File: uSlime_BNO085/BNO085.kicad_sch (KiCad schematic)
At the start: 12 parts, among them CN1 X1502WR-05K-N0SN, U1 BNO085

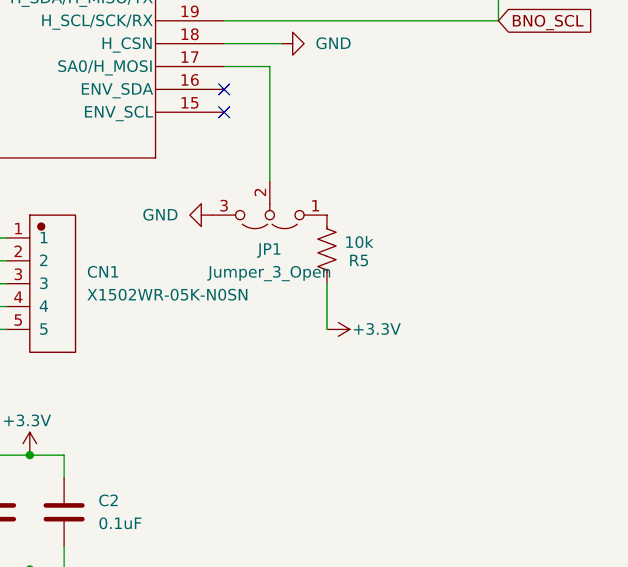
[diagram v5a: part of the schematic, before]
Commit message: Connect DI without resistor
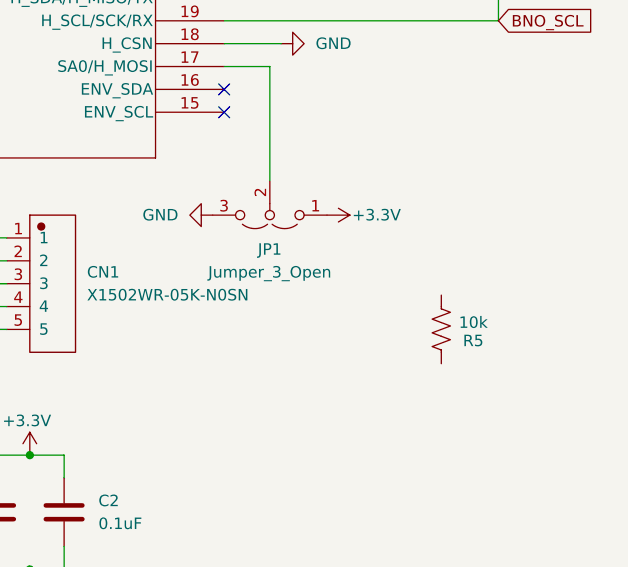
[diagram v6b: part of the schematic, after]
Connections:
- net +3.3V: now also JP1.1 (A); no longer R5.2
- net at R5.1: no longer JP1.1 (A)
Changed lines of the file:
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@@
-	(wire
-		(pts
-			(xy 168.91 119.38) (xy 168.91 114.3)
-		)
-		(stroke
-			(width 0)
-			(type default)
-		)
-	)
 	(wire
 		(pts
@@
 	(symbol
 		(lib_id "power:+3.3V")
-		(at 168.91 119.38 270)
+		(at 168.91 106.68 270)
 		(unit 1)
 		(exclude_from_sim no)
@@
 		(dnp no)
 		(property "Reference" "#PWR014"
-			(at 165.1 119.38 0)
+			(at 165.1 106.68 0)
 			(effects
 				(font
@@
 		)
 		(property "Value" "+3.3V"
-			(at 171.704 119.38 90)
+			(at 171.704 106.68 90)
 			(effects
 				(font
@@
 		)
 		(property "Footprint" ""
-			(at 168.91 119.38 0)
+			(at 168.91 106.68 0)
 			(effects
 				(font
@@
 		)
 		(property "Datasheet" ""
-			(at 168.91 119.38 0)
+			(at 168.91 106.68 0)
 			(effects
 				(font
@@
 		)
 		(property "Description" "Power symbol creates a global label with name \"+3.3V\""
-			(at 168.91 119.38 0)
+			(at 168.91 106.68 0)
 			(effects
 				(font
@@
 				(path "/f32c1c49-f803-4e7c-a530-6db148a7ba36/1072de81-ddaf-4115-9b1e-8b480e2a0117"
 					(reference "#PWR014")
-					(unit 1)
-				)
-			)
-		)
-	)
-	(symbol
-		(lib_id "uSlime:R_US")
-		(at 168.91 110.49 0)
-		(unit 1)
-		(exclude_from_sim no)
-		(in_bom yes)
-		(on_board yes)
-		(dnp no)
-		(property "Reference" "R5"
-			(at 172.466 111.76 0)
-			(effects
-				(font
-					(size 1.27 1.27)
-				)
-			)
-		)
-		(property "Value" "10k"
-			(at 172.466 109.728 0)
-			(effects
-				(font
-					(size 1.27 1.27)
-				)
-			)
-		)
-		(property "Footprint" "Resistor_SMD:R_0402_1005Metric"
-			(at 169.926 110.744 90)
-			(effects
-				(font
-					(size 1.27 1.27)
-				)
-				(hide yes)
-			)
-		)
-		(property "Datasheet" "~"
-			(at 168.91 110.49 0)
-			(effects
-				(font
-					(size 1.27 1.27)
-				)
-				(hide yes)
-			)
-		)
-		(property "Description" "Resistor, US symbol"
-			(at 168.91 110.49 0)
-			(effects
-				(font
-					(size 1.27 1.27)
-				)
-				(hide yes)
-			)
-		)
-		(pin "2"
-		)
-		(pin "1"
-		)
-		(instances
-			(project "uSlime_BNO085"
-				(path "/f32c1c49-f803-4e7c-a530-6db148a7ba36/1072de81-ddaf-4115-9b1e-8b480e2a0117"
-					(reference "R5")
 					(unit 1)
 				)
@@
 					(unit 1)
 				)
+			)
+		)
+	)
+	(symbol
+		(lib_id "uSlime:R_US")
+		(at 181.61 119.38 0)
+		(unit 1)
+		(exclude_from_sim no)
+		(in_bom yes)
+		(on_board yes)
+		(dnp no)
+		(property "Reference" "R5"
+			(at 185.166 120.65 0)
+			(effects
+				(font
+					(size 1.27 1.27)
+				)
+			)
+		)
+		(property "Value" "10k"
+			(at 185.166 118.618 0)
+			(effects
+				(font
+					(size 1.27 1.27)
+				)
+			)
+		)
+		(property "Footprint" "Resistor_SMD:R_0402_1005Metric"
+			(at 182.626 119.634 90)
+			(effects
+				(font
+					(size 1.27 1.27)
+				)
+				(hide yes)
+			)
+		)
+		(property "Datasheet" "~"
+			(at 181.61 119.38 0)
+			(effects
+				(font
+					(size 1.27 1.27)
+				)
+				(hide yes)
+			)
+		)
+		(property "Description" "Resistor, US symbol"
+			(at 181.61 119.38 0)
+			(effects
+				(font
+					(size 1.27 1.27)
+				)
+				(hide yes)
+			)
+		)
+		(pin "2"
+		)
+		(pin "1"
+		)
+		(instances
+			(project "uSlime_BNO085"
+				(path "/f32c1c49-f803-4e7c-a530-6db148a7ba36/1072de81-ddaf-4115-9b1e-8b480e2a0117"
+					(reference "R5")
+					(unit 1)
+				)

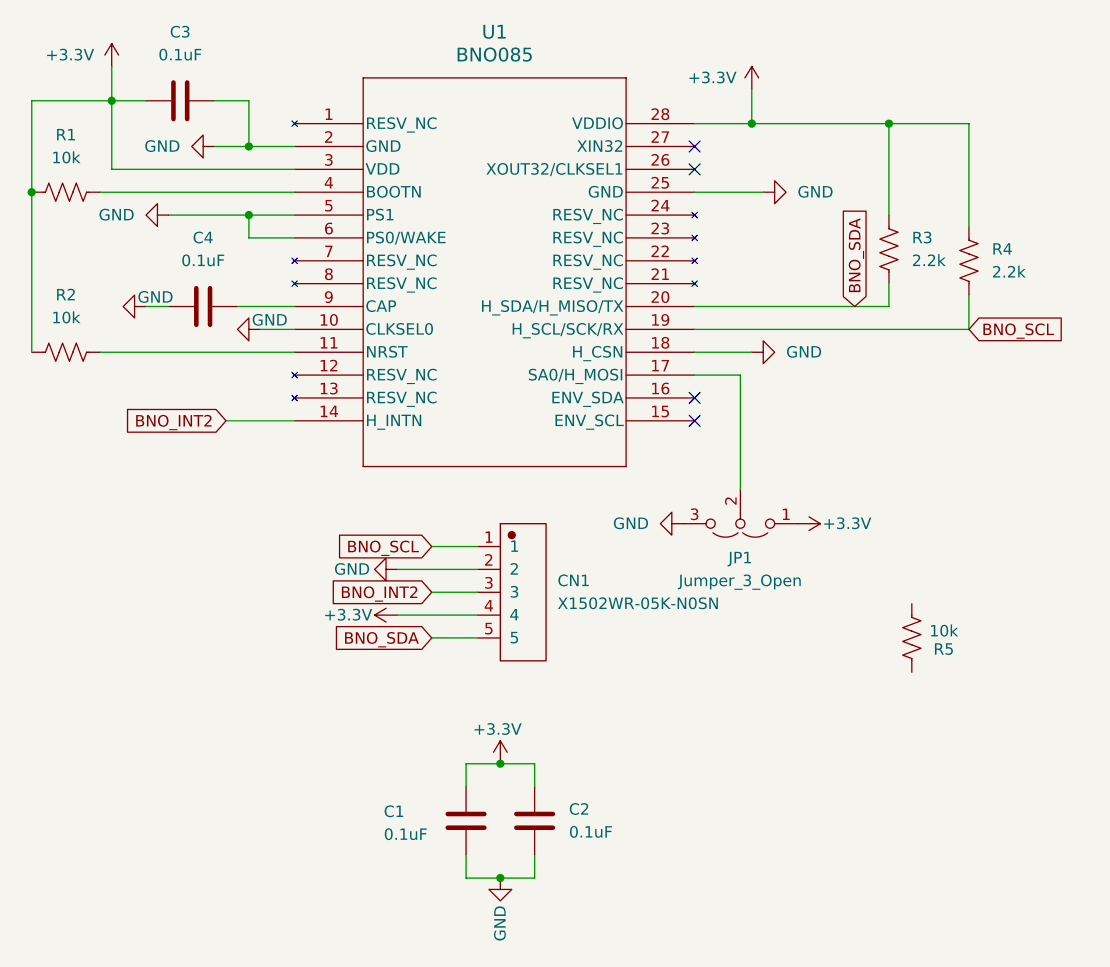
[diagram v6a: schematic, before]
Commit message: v0.0.5: Invert CLKSEL pin to 3.3V
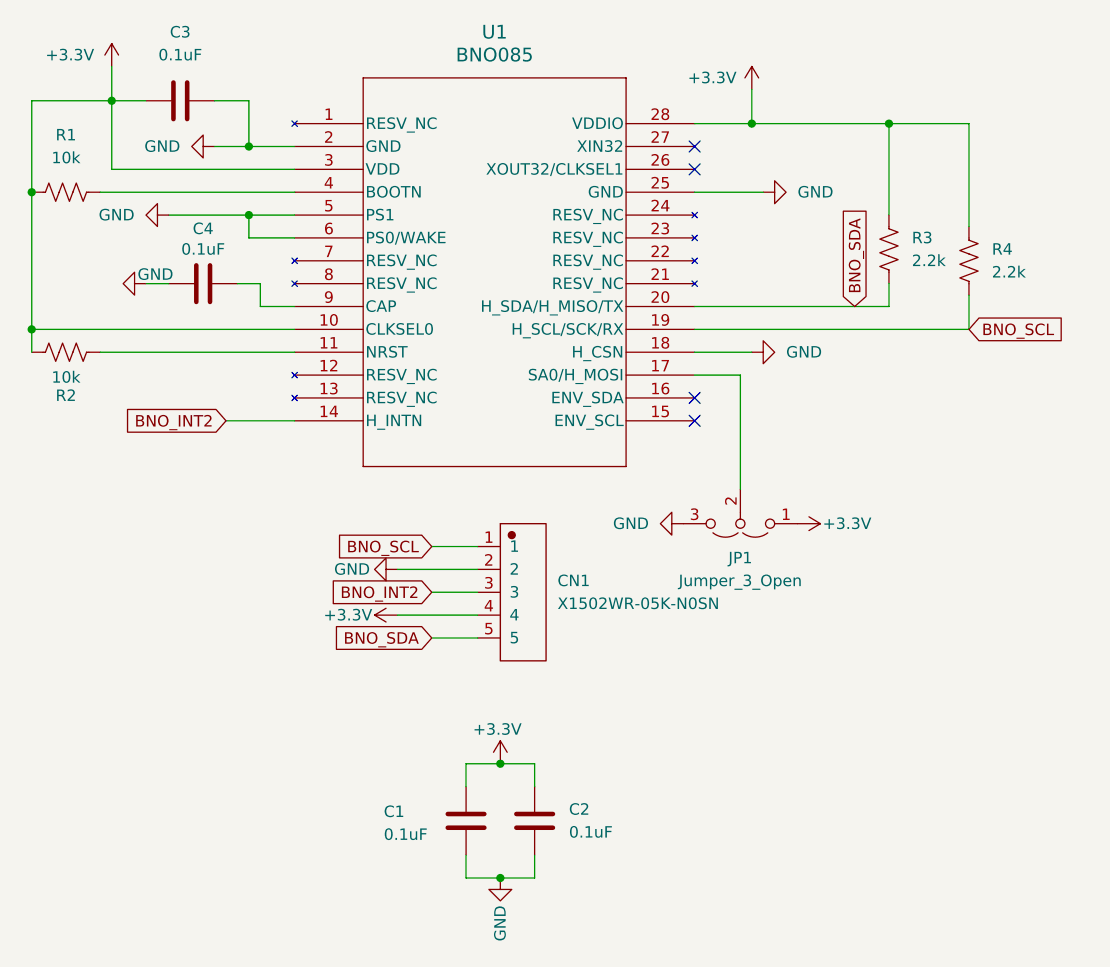
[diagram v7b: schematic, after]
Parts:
- removed R5: 10k, Resistor_SMD:R_0402_1005Metric, symbol uSlime:R_US
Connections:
- net +3.3V: now also U1.10 (CLKSEL0)
- net GND: no longer U1.10 (CLKSEL0)
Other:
- moved on the sheet: C4
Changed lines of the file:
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@@
+		(color 0 0 0 0)
+	)
+	(junction
+		(at 83.82 85.09)
+		(diameter 0)
 		(color 0 0 0 0)
 	)
@@
 	(wire
 		(pts
+			(xy 96.52 80.01) (xy 99.06 80.01)
+		)
+		(stroke
+			(width 0)
+			(type default)
+		)
+	)
+	(wire
+		(pts
+			(xy 109.22 82.55) (xy 113.03 82.55)
+		)
+		(stroke
+			(width 0)
+			(type default)
+		)
+	)
+	(wire
+		(pts
 			(xy 104.14 64.77) (xy 107.95 64.77)
 		)
@@
 	(wire
 		(pts
-			(xy 96.52 82.55) (xy 99.06 82.55)
-		)
-		(stroke
-			(width 0)
-			(type default)
-		)
-	)
-	(wire
-		(pts
 			(xy 92.71 59.69) (xy 92.71 67.31)
 		)
@@
 	(wire
 		(pts
+			(xy 83.82 85.09) (xy 83.82 87.63)
+		)
+		(stroke
+			(width 0)
+			(type default)
+		)
+	)
+	(wire
+		(pts
 			(xy 124.46 111.76) (xy 133.35 111.76)
 		)
@@
 	(wire
 		(pts
-			(xy 83.82 69.85) (xy 83.82 87.63)
+			(xy 83.82 69.85) (xy 83.82 85.09)
 		)
 		(stroke
@@
 	(wire
 		(pts
+			(xy 83.82 85.09) (xy 113.03 85.09)
+		)
+		(stroke
+			(width 0)
+			(type default)
+		)
+	)
+	(wire
+		(pts
 			(xy 107.95 72.39) (xy 113.03 72.39)
 		)
@@
 	(wire
 		(pts
-			(xy 109.22 85.09) (xy 113.03 85.09)
-		)
-		(stroke
-			(width 0)
-			(type default)
-		)
-	)
-	(wire
-		(pts
 			(xy 107.95 64.77) (xy 113.03 64.77)
 		)
@@
 	(wire
 		(pts
-			(xy 106.68 82.55) (xy 113.03 82.55)
+			(xy 106.68 80.01) (xy 109.22 80.01)
 		)
 		(stroke
@@
 		(pts
 			(xy 124.46 116.84) (xy 133.35 116.84)
+		)
+		(stroke
+			(width 0)
+			(type default)
+		)
+	)
+	(wire
+		(pts
+			(xy 109.22 80.01) (xy 109.22 82.55)
 		)
 		(stroke
@@
 	(symbol
 		(lib_id "power:GND")
-		(at 96.52 82.55 270)
+		(at 96.52 80.01 270)
 		(unit 1)
 		(exclude_from_sim no)
@@
 		(dnp no)
 		(property "Reference" "#PWR02"
-			(at 90.17 82.55 0)
+			(at 90.17 80.01 0)
 			(effects
 				(font
@@
 		)
 		(property "Value" "GND"
-			(at 99.568 81.534 90)
+			(at 99.568 78.994 90)
 			(effects
 				(font
@@
 		)
 		(property "Footprint" ""
-			(at 96.52 82.55 0)
+			(at 96.52 80.01 0)
 			(effects
 				(font
@@
 		)
 		(property "Datasheet" ""
-			(at 96.52 82.55 0)
+			(at 96.52 80.01 0)
 			(effects
 				(font
@@
 		)
 		(property "Description" "Power symbol creates a global label with name \"GND\" , ground"
-			(at 96.52 82.55 0)
+			(at 96.52 80.01 0)
 			(effects
 				(font
@@
 	(symbol
 		(lib_id "power:GND")
-		(at 109.22 85.09 270)
-		(unit 1)
-		(exclude_from_sim no)
-		(in_bom yes)
-		(on_board yes)
-		(dnp no)
-		(property "Reference" "#PWR07"
-			(at 102.87 85.09 0)
-			(effects
-				(font
-					(size 1.27 1.27)
-				)
-				(hide yes)
-			)
-		)
-		(property "Value" "GND"
-			(at 112.268 84.074 90)
-			(effects
-				(font
-					(size 1.27 1.27)
-				)
-				(justify right)
-			)
-		)
-		(property "Footprint" ""
-			(at 109.22 85.09 0)
-			(effects
-				(font
-					(size 1.27 1.27)
-				)
-				(hide yes)
-			)
-		)
-		(property "Datasheet" ""
-			(at 109.22 85.09 0)
-			(effects
-				(font
-					(size 1.27 1.27)
-				)
-				(hide yes)
-			)
-		)
-		(property "Description" "Power symbol creates a global label with name \"GND\" , ground"
-			(at 109.22 85.09 0)
-			(effects
-				(font
-					(size 1.27 1.27)
-				)
-				(hide yes)
-			)
-		)
-		(pin "1"
-		)
-		(instances
-			(project "uSlime_BNO085"
-				(path "/f32c1c49-f803-4e7c-a530-6db148a7ba36/1072de81-ddaf-4115-9b1e-8b480e2a0117"
-					(reference "#PWR07")
-					(unit 1)
-				)
-			)
-		)
-	)
-	(symbol
-		(lib_id "power:GND")
 		(at 99.06 72.39 270)
 		(unit 1)
@@
 	(symbol
 		(lib_id "uSlime:R_US")
-		(at 181.61 119.38 0)
-		(unit 1)
-		(exclude_from_sim no)
-		(in_bom yes)
-		(on_board yes)
-		(dnp no)
-		(property "Reference" "R5"
-			(at 185.166 120.65 0)
-			(effects
-				(font
-					(size 1.27 1.27)
-				)
-			)
-		)
-		(property "Value" "10k"
-			(at 185.166 118.618 0)
-			(effects
-				(font
-					(size 1.27 1.27)
-				)
-			)
-		)
-		(property "Footprint" "Resistor_SMD:R_0402_1005Metric"
-			(at 182.626 119.634 90)
-			(effects
-				(font
-					(size 1.27 1.27)
-				)
-				(hide yes)
-			)
-		)
-		(property "Datasheet" "~"
-			(at 181.61 119.38 0)
-			(effects
-				(font
-					(size 1.27 1.27)
-				)
-				(hide yes)
-			)
-		)
-		(property "Description" "Resistor, US symbol"
-			(at 181.61 119.38 0)
-			(effects
-				(font
-					(size 1.27 1.27)
-				)
-				(hide yes)
-			)
-		)
-		(pin "2"
-		)
-		(pin "1"
-		)
-		(instances
-			(project "uSlime_BNO085"
-				(path "/f32c1c49-f803-4e7c-a530-6db148a7ba36/1072de81-ddaf-4115-9b1e-8b480e2a0117"
-					(reference "R5")
-					(unit 1)
-				)
-			)
-		)
-	)
-	(symbol
-		(lib_id "uSlime:R_US")
 		(at 87.63 69.85 90)
 		(unit 1)
@@
 	(symbol
 		(lib_id "uSlime:C")
-		(at 102.87 82.55 90)
+		(at 102.87 80.01 90)
 		(unit 1)
 		(exclude_from_sim no)
@@
 		(on_board yes)
 		(dnp no)
-		(fields_autoplaced yes)
 		(property "Reference" "C4"
-			(at 102.87 74.93 90)
+			(at 102.87 73.914 90)
 			(effects
 				(font
@@
 		)
 		(property "Value" "0.1uF"
-			(at 102.87 77.47 90)
+			(at 102.87 76.2 90)
 			(effects
 				(font
@@
 		)
 		(property "Footprint" "Capacitor_SMD:C_0402_1005Metric"
-			(at 106.68 81.5848 0)
+			(at 106.68 79.0448 0)
 			(effects
 				(font
@@
 		)
 		(property "Datasheet" "~"
-			(at 102.87 82.55 0)
+			(at 102.87 80.01 0)
 			(effects
 				(font
@@
 		)
 		(property "Description" "Unpolarized capacitor"
-			(at 102.87 82.55 0)
+			(at 102.87 80.01 0)
 			(effects
 				(font
@@
 		(on_board yes)
 		(dnp no)
-		(fields_autoplaced yes)
 		(property "Reference" "R2"
-			(at 87.63 81.28 90)
+			(at 87.63 92.456 90)
 			(effects
 				(font
@@
 		)
 		(property "Value" "10k"
-			(at 87.63 83.82 90)
-			(effects
-				(font
+			(at 87.63 90.424 90)
+			(effects
+				(font

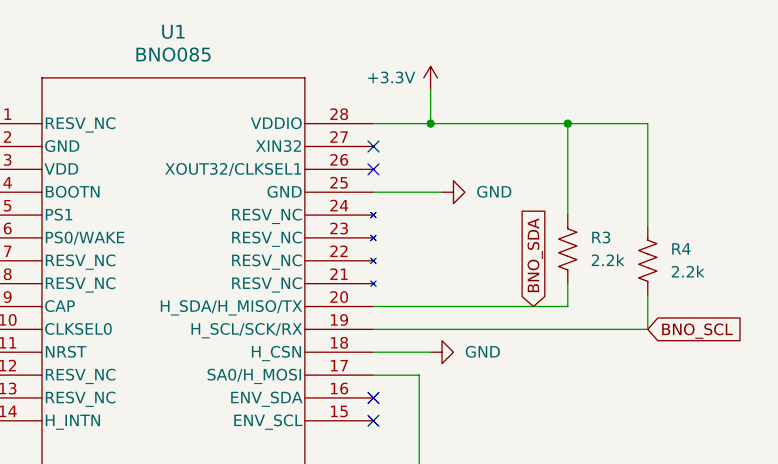
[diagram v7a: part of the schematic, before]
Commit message: Connect pin 26 to GND
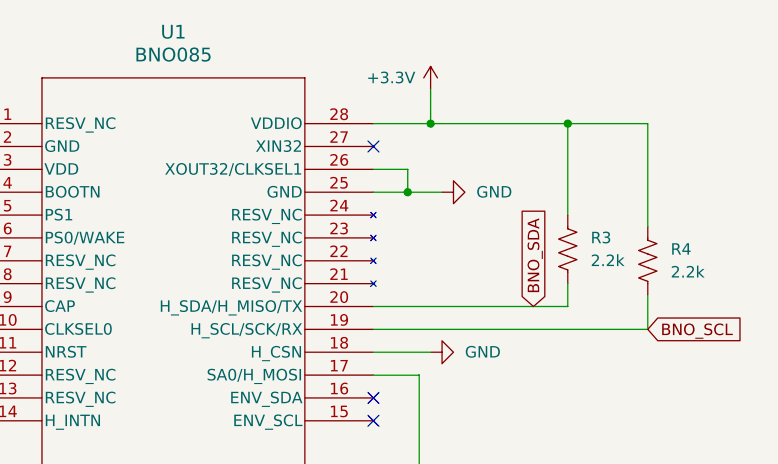
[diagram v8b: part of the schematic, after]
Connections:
- net GND: now also U1.26 (XOUT32/CLKSEL1)
- no-connect marks 4 -> 3
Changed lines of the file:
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@@
+	)
+	(junction
+		(at 161.29 69.85)
+		(diameter 0)
+		(color 0 0 0 0)
 	)
 	(junction
@@
 	)
 	(no_connect
-		(at 157.48 67.31)
-	)
-	(no_connect
 		(at 157.48 95.25)
 	)
@@
 	(wire
 		(pts
+			(xy 161.29 67.31) (xy 161.29 69.85)
+		)
+		(stroke
+			(width 0)
+			(type default)
+		)
+	)
+	(wire
+		(pts
 			(xy 91.44 69.85) (xy 113.03 69.85)
 		)
@@
 	(wire
 		(pts
-			(xy 165.1 69.85) (xy 157.48 69.85)
+			(xy 165.1 69.85) (xy 161.29 69.85)
 		)
 		(stroke
@@
 	(wire
 		(pts
+			(xy 157.48 67.31) (xy 161.29 67.31)
+		)
+		(stroke
+			(width 0)
+			(type default)
+		)
+	)
+	(wire
+		(pts
 			(xy 132.08 146.05) (xy 135.89 146.05)
 		)
@@
 		)
 		(stroke
+			(width 0)
+			(type default)
+		)
+	)
+	(wire
+		(pts
+			(xy 161.29 69.85) (xy 157.48 69.85)
+		)
+		(stroke
